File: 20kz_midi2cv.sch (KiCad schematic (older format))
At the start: 27 parts, among them J1 DIN_5, J2 TONE, J3 GATE, J4 GATE, J5 PITCH BEND, J6 power, Q1 2N3904, Q2 2N3904, U1 4N35, U2 ATMEGA328P-PU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

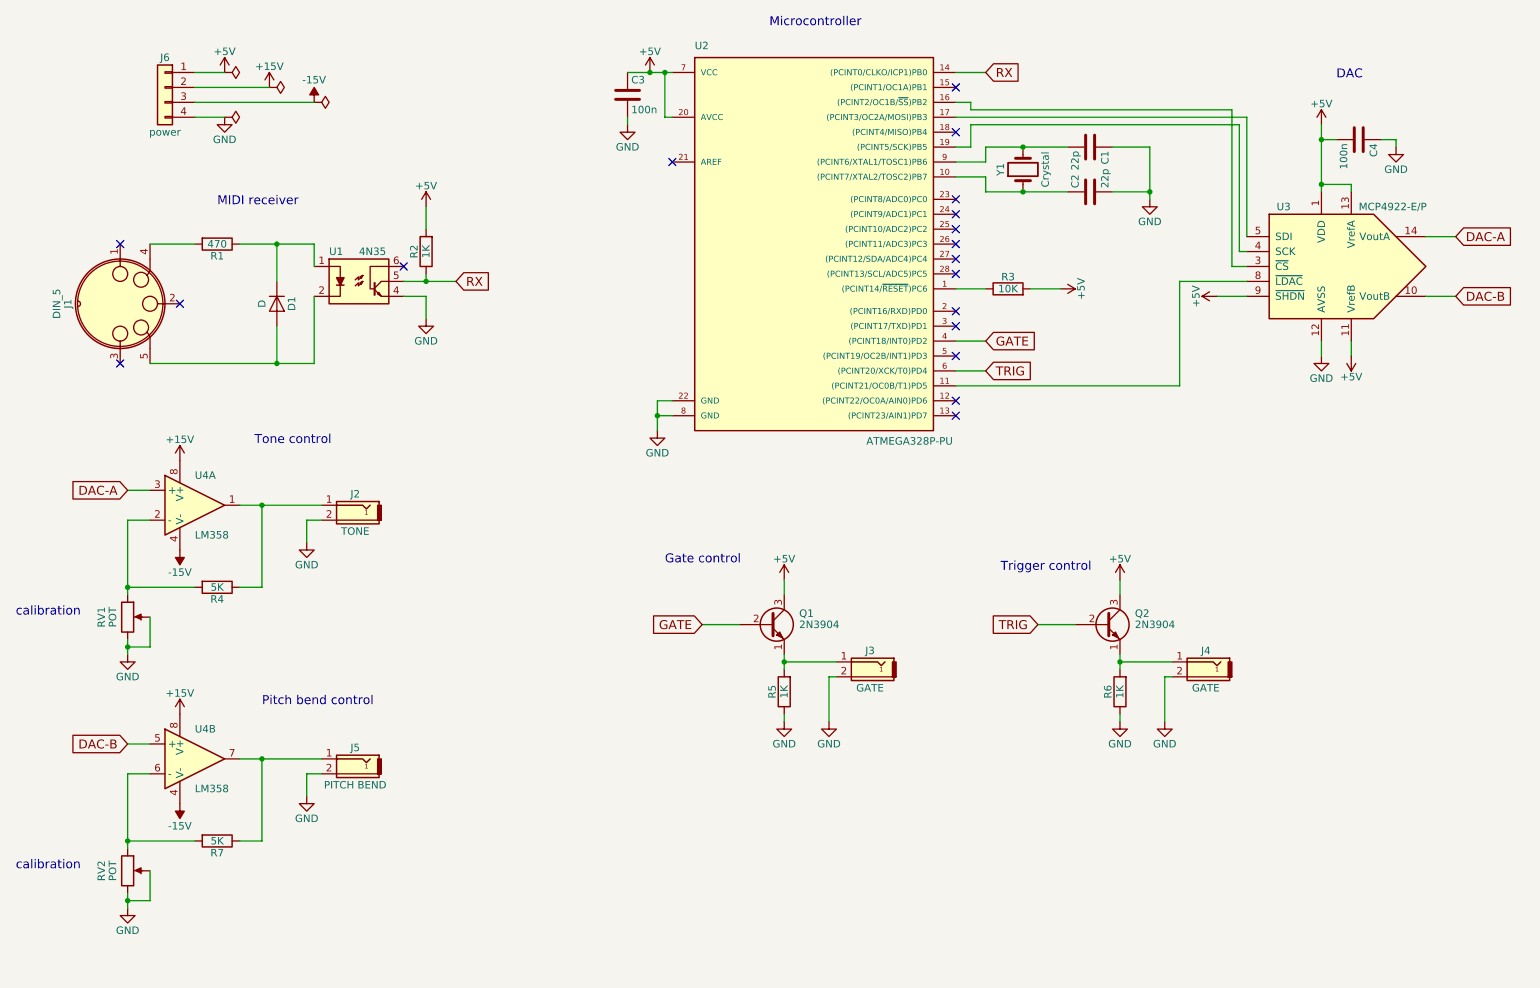
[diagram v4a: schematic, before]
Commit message: el pitch bend control no necesita opamp
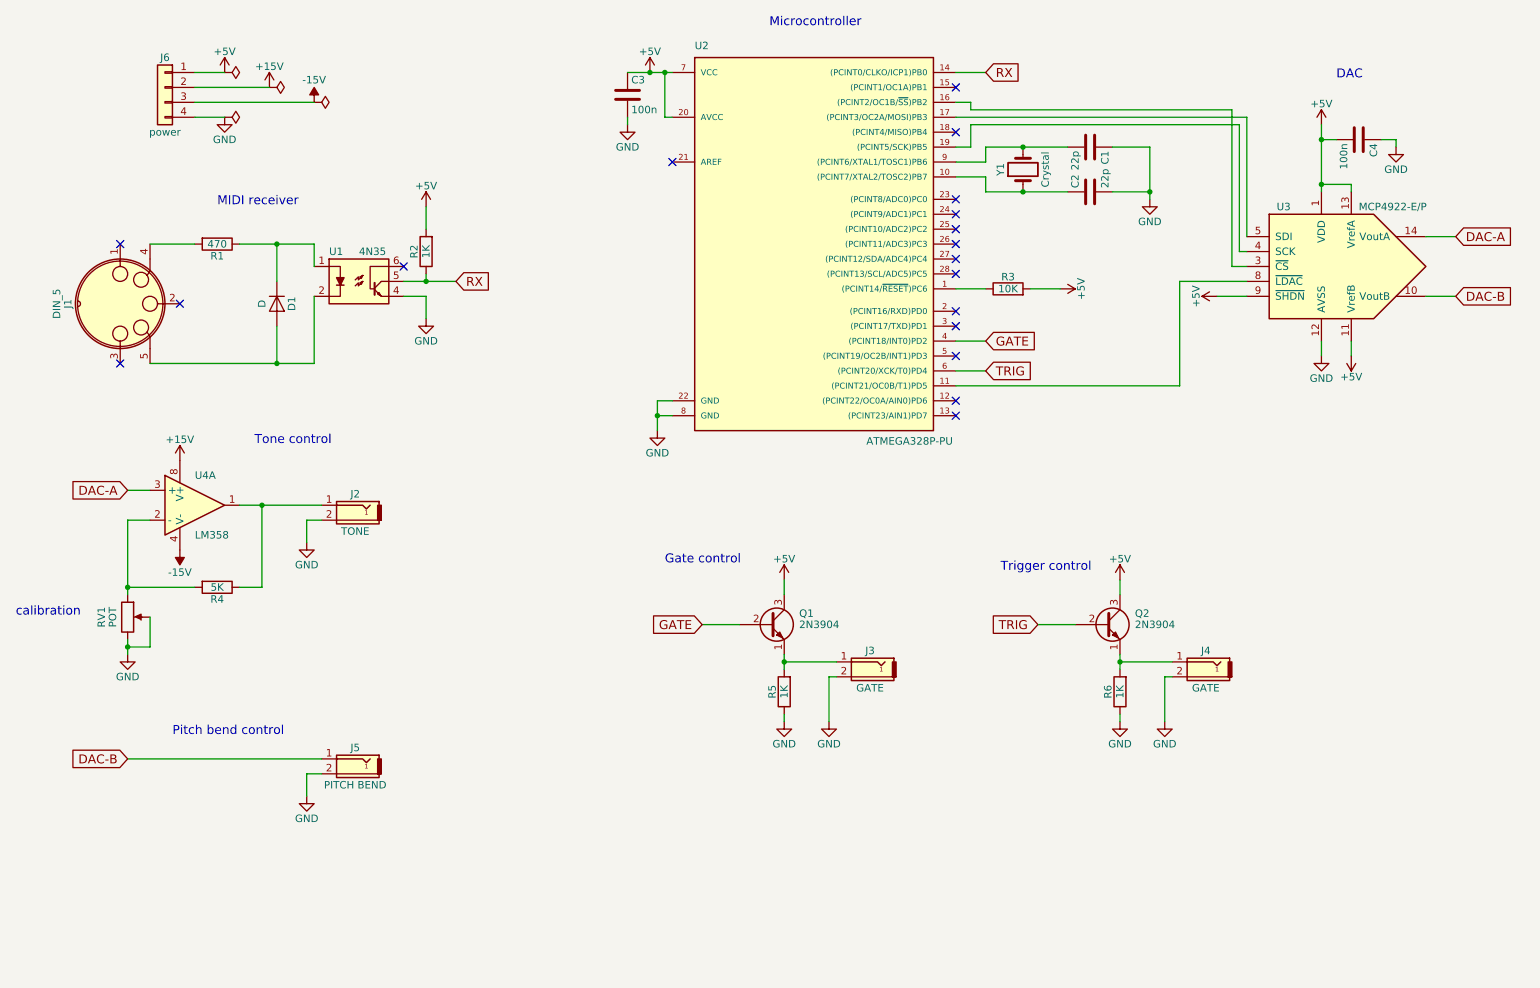
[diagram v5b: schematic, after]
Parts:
- removed R7: 5K, symbol R
- removed RV2: POT, symbol POT
- removed unit 2 of U4
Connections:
- net DAC-B: now also J5.1
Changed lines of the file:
@@
 $EndComp
 $Comp
-L GND #PWR13
+L GND #PWR01
 U 1 1 59BFD3CC
 P 3450 2800
-F 0 "#PWR13" H 3450 2550 50  0001 C CNN
+F 0 "#PWR01" H 3450 2550 50  0001 C CNN
 F 1 "GND" H 3450 2650 50  0000 C CNN
 F 2 "" H 3450 2800 50  0001 C CNN
@@
 $EndComp
 $Comp
-L GND #PWR16
+L GND #PWR02
 U 1 1 59BFDB2E
 P 5000 3550
-F 0 "#PWR16" H 5000 3300 50  0001 C CNN
+F 0 "#PWR02" H 5000 3300 50  0001 C CNN
 F 1 "GND" H 5000 3400 50  0000 C CNN
 F 2 "" H 5000 3550 50  0001 C CNN
@@
 $EndComp
 $Comp
-L GND #PWR9
+L GND #PWR03
 U 1 1 59BFF0AF
 P 8300 2000
-F 0 "#PWR9" H 8300 1750 50  0001 C CNN
+F 0 "#PWR03" H 8300 1750 50  0001 C CNN
 F 1 "GND" H 8300 1850 50  0000 C CNN
 F 2 "" H 8300 2000 50  0001 C CNN
@@
 RX
 $Comp
-L GND #PWR14
+L GND #PWR04
 U 1 1 59C28A87
 P 9450 3050
-F 0 "#PWR14" H 9450 2800 50  0001 C CNN
+F 0 "#PWR04" H 9450 2800 50  0001 C CNN
 F 1 "GND" H 9450 2900 50  0000 C CNN
 F 2 "" H 9450 3050 50  0001 C CNN
@@
 Microcontroller
 $Comp
-L +5V #PWR10
+L +5V #PWR05
 U 1 1 59C2B213
 P 3450 2050
-F 0 "#PWR10" H 3450 1900 50  0001 C CNN
+F 0 "#PWR05" H 3450 1900 50  0001 C CNN
 F 1 "+5V" H 3450 2190 50  0000 C CNN
 F 2 "" H 3450 2050 50  0001 C CNN
@@
 $EndComp
 $Comp
-L +5V #PWR2
+L +5V #PWR06
 U 1 1 59C2B4B2
 P 4950 1150
-F 0 "#PWR2" H 4950 1000 50  0001 C CNN
+F 0 "#PWR06" H 4950 1000 50  0001 C CNN
 F 1 "+5V" H 4950 1290 50  0000 C CNN
 F 2 "" H 4950 1150 50  0001 C CNN
@@
 $EndComp
 $Comp
-L +5V #PWR7
+L +5V #PWR07
 U 1 1 59C2B740
 P 9450 1500
-F 0 "#PWR7" H 9450 1350 50  0001 C CNN
+F 0 "#PWR07" H 9450 1350 50  0001 C CNN
 F 1 "+5V" H 9450 1640 50  0000 C CNN
 F 2 "" H 9450 1500 50  0001 C CNN
@@
 $EndComp
 $Comp
-L +5V #PWR15
+L +5V #PWR08
 U 1 1 59C2B949
 P 9650 3050
-F 0 "#PWR15" H 9650 2900 50  0001 C CNN
+F 0 "#PWR08" H 9650 2900 50  0001 C CNN
 F 1 "+5V" H 9650 3190 50  0000 C CNN
 F 2 "" H 9650 3050 50  0001 C CNN
@@
 $EndComp
 $Comp
-L +5V #PWR11
+L +5V #PWR09
 U 1 1 59C2BF25
 P 7700 2600
-F 0 "#PWR11" H 7700 2450 50  0001 C CNN
+F 0 "#PWR09" H 7700 2450 50  0001 C CNN
 F 1 "+5V" H 7700 2740 50  0000 C CNN
 F 2 "" H 7700 2600 50  0001 C CNN
@@
 $EndComp
 $Comp
-L +5V #PWR12
+L +5V #PWR010
 U 1 1 59C2C020
 P 8750 2650
-F 0 "#PWR12" H 8750 2500 50  0001 C CNN
+F 0 "#PWR010" H 8750 2500 50  0001 C CNN
 F 1 "+5V" H 8750 2790 50  0000 C CNN
 F 2 "" H 8750 2650 50  0001 C CNN
@@
 Connection ~ 9450 1900
 Wire Wire Line
-	9650 1900 9450 1900
+	9450 1900 9650 1900
 Wire Wire Line
 	9650 1950 9650 1900
@@
 $EndComp
 $Comp
-L +15V #PWR17
+L +15V #PWR011
 U 1 1 59C3649C
 P 1800 3750
-F 0 "#PWR17" H 1800 3600 50  0001 C CNN
+F 0 "#PWR011" H 1800 3600 50  0001 C CNN
 F 1 "+15V" H 1800 3890 50  0000 C CNN
 F 2 "" H 1800 3750 50  0001 C CNN
@@
 	10150 2250 10350 2250
 $Comp
-L GND #PWR22
+L GND #PWR012
 U 1 1 59C37211
 P 1450 5050
-F 0 "#PWR22" H 1450 4800 50  0001 C CNN
+F 0 "#PWR012" H 1450 4800 50  0001 C CNN
 F 1 "GND" H 1450 4900 50  0000 C CNN
 F 2 "" H 1450 5050 50  0001 C CNN
@@
 Connection ~ 2350 4050
 $Comp
-L GND #PWR18
+L GND #PWR013
 U 1 1 59C38A05
 P 2650 4300
-F 0 "#PWR18" H 2650 4050 50  0001 C CNN
+F 0 "#PWR013" H 2650 4050 50  0001 C CNN
 F 1 "GND" H 2650 4150 50  0000 C CNN
 F 2 "" H 2650 4300 50  0001 C CNN
@@
 Wire Wire Line
 	2650 4150 2650 4300
-$Comp
-L LM358 U4
-U 2 1 59C38F55
-P 1900 5750
-F 0 "U4" H 1900 5950 50  0000 L CNN
-F 1 "LM358" H 1900 5550 50  0000 L CNN
-F 2 "" H 1900 5750 50  0001 C CNN
-F 3 "" H 1900 5750 50  0001 C CNN
-	2    1900 5750
-	1    0    0    -1
-$EndComp
-$Comp
-L +15V #PWR23
-U 1 1 59C38F5B
-P 1800 5450
-F 0 "#PWR23" H 1800 5300 50  0001 C CNN
-F 1 "+15V" H 1800 5590 50  0000 C CNN
-F 2 "" H 1800 5450 50  0001 C CNN
-F 3 "" H 1800 5450 50  0001 C CNN
-	1    1800 5450
-	1    0    0    -1
-$EndComp
-$Comp
-L -15V #PWR29
-U 1 1 59C38F61
-P 1800 6050
-F 0 "#PWR29" H 1800 6150 50  0001 C CNN
-F 1 "-15V" H 1800 6200 50  0000 C CNN
-F 2 "" H 1800 6050 50  0001 C CNN
-F 3 "" H 1800 6050 50  0001 C CNN
-	1    1800 6050
-	-1   0    0    1
-$EndComp
-Wire Wire Line
-	1800 5450 1800 5450
-Wire Wire Line
-	1800 6050 1800 6050
-$Comp
-L R R7
-U 1 1 59C38F69
-P 2050 6300
-F 0 "R7" V 2130 6300 50  0000 C CNN
-F 1 "5K" V 2050 6300 50  0000 C CNN
-F 2 "" V 1980 6300 50  0001 C CNN
-F 3 "" H 2050 6300 50  0001 C CNN
-	1    2050 6300
-	0    1    1    0
-$EndComp
-$Comp
-L POT RV2
-U 1 1 59C38F6F
-P 1450 6500
-F 0 "RV2" V 1275 6500 50  0000 C CNN
-F 1 "POT" V 1350 6500 50  0000 C CNN
-F 2 "" H 1450 6500 50  0001 C CNN
-F 3 "" H 1450 6500 50  0001 C CNN
-	1    1450 6500
-	1    0    0    -1
-$EndComp
-$Comp
-L GND #PWR30
-U 1 1 59C38F75
-P 1450 6750
-F 0 "#PWR30" H 1450 6500 50  0001 C CNN
-F 1 "GND" H 1450 6600 50  0000 C CNN
-F 2 "" H 1450 6750 50  0001 C CNN
-F 3 "" H 1450 6750 50  0001 C CNN
-	1    1450 6750
-	1    0    0    -1
-$EndComp
-Wire Wire Line
-	1450 6650 1450 6750
-Wire Wire Line
-	1600 6500 1600 6700
-Wire Wire Line
-	1600 6700 1450 6700
-Connection ~ 1450 6700
-Wire Wire Line
-	1600 5850 1450 5850
-Wire Wire Line
-	1450 5850 1450 6350
-Wire Wire Line
-	1900 6300 1450 6300
-Connection ~ 1450 6300
-Wire Wire Line
-	2200 5750 2750 5750
-Wire Wire Line
-	2350 5750 2350 6300
-Wire Wire Line
-	2350 6300 2200 6300
-Wire Wire Line
-	1600 5650 1450 5650
 $Comp
 L Audio-Jack-2 J5
@@
 	-1   0    0    -1
 $EndComp
-Connection ~ 2350 5750
-$Comp
-L GND #PWR28
+$Comp
+L GND #PWR016
 U 1 1 59C38F8F
 P 2650 6000
-F 0 "#PWR28" H 2650 5750 50  0001 C CNN
+F 0 "#PWR016" H 2650 5750 50  0001 C CNN
 F 1 "GND" H 2650 5850 50  0000 C CNN
 F 2 "" H 2650 6000 50  0001 C CNN
@@
 Wire Wire Line
 	2650 5850 2650 6000
-Text GLabel 1450 5650 0    60   Input ~ 0
+Text GLabel 1450 5750 0    60   Input ~ 0
 DAC-B
 Text GLabel 7200 2950 2    60   Input ~ 0
@@
 $EndComp
 $Comp
-L GND #PWR24
+L GND #PWR017
 U 1 1 59C39D84
 P 5850 5500
-F 0 "#PWR24" H 5850 5250 50  0001 C CNN
+F 0 "#PWR017" H 5850 5250 50  0001 C CNN
 F 1 "GND" H 5850 5350 50  0000 C CNN
 F 2 "" H 5850 5500 50  0001 C CNN
@@
 $EndComp
 $Comp
-L +5V #PWR20
+L +5V #PWR018
 U 1 1 59C3A03A
 P 5850 4550
-F 0 "#PWR20" H 5850 4400 50  0001 C CNN
+F 0 "#PWR018" H 5850 4400 50  0001 C CNN
 F 1 "+5V" H 5850 4690 50  0000 C CNN
 F 2 "" H 5850 4550 50  0001 C CNN
@@
 Connection ~ 5850 5100
 $Comp
-L GND #PWR25
+L GND #PWR019
 U 1 1 59C3A4C6
 P 6150 5500
-F 0 "#PWR25" H 6150 5250 50  0001 C CNN
+F 0 "#PWR019" H 6150 5250 50  0001 C CNN
 F 1 "GND" H 6150 5350 50  0000 C CNN
 F 2 "" H 6150 5500 50  0001 C CNN
@@
 $EndComp
 $Comp
-L GND #PWR26
+L GND #PWR020
 U 1 1 59C3A967
 P 8100 5500
-F 0 "#PWR26" H 8100 5250 50  0001 C CNN
+F 0 "#PWR020" H 8100 5250 50  0001 C CNN
 F 1 "GND" H 8100 5350 50  0000 C CNN
 F 2 "" H 8100 5500 50  0001 C CNN
@@
 $EndComp
 $Comp
-L +5V #PWR21
+L +5V #PWR021
 U 1 1 59C3A973
 P 8100 4550
-F 0 "#PWR21" H 8100 4400 50  0001 C CNN
+F 0 "#PWR021" H 8100 4400 50  0001 C CNN
 F 1 "+5V" H 8100 4690 50  0000 C CNN
 F 2 "" H 8100 4550 50  0001 C CNN
@@
 Connection ~ 8100 5100
 $Comp
-L GND #PWR27
+L GND #PWR022
 U 1 1 59C3A985
 P 8400 5500
-F 0 "#PWR27" H 8400 5250 50  0001 C CNN
+F 0 "#PWR022" H 8400 5250 50  0001 C CNN
 F 1 "GND" H 8400 5350 50  0000 C CNN
 F 2 "" H 8400 5500 50  0001 C CNN
@@
 Text Notes 2300 3650 0    60   ~ 0
 Tone control
-Text Notes 2350 5400 0    60   ~ 0
+Text Notes 1750 5600 0    60   ~ 0
 Pitch bend control
 Text Notes 5050 4450 0    60   ~ 0
@@
 Text Notes 7300 4500 0    60   ~ 0
 Trigger control
-Text Notes 700  6500 0    60   ~ 0
-calibration
 Text Notes 700  4800 0    60   ~ 0
 calibration
@@
 $EndComp
 $Comp
-L +5V #PWR1
+L +5V #PWR023
 U 1 1 59C3CE9F
 P 2100 1150
-F 0 "#PWR1" H 2100 1000 50  0001 C CNN
+F 0 "#PWR023" H 2100 1000 50  0001 C CNN
 F 1 "+5V" H 2100 1290 50  0000 C CNN
 F 2 "" H 2100 1150 50  0001 C CNN
@@
 $EndComp
 $Comp
-L +15V #PWR3
+L +15V #PWR024
 U 1 1 59C3CF60
 P 2400 1250
-F 0 "#PWR3" H 2400 1100 50  0001 C CNN
+F 0 "#PWR024" H 2400 1100 50  0001 C CNN
 F 1 "+15V" H 2400 1390 50  0000 C CNN
 F 2 "" H 2400 1250 50  0001 C CNN
@@
 $EndComp
 $Comp
-L GND #PWR5
+L GND #PWR025
 U 1 1 59C3D43E
 P 2100 1450
-F 0 "#PWR5" H 2100 1200 50  0001 C CNN
+F 0 "#PWR025" H 2100 1200 50  0001 C CNN
 F 1 "GND" H 2100 1300 50  0000 C CNN
 F 2 "" H 2100 1450 50  0001 C CNN
@@
 	1900 1450 2100 1450
 $Comp
-L PWR_FLAG #FLG1
+L PWR_FLAG #FLG026
 U 1 1 59C3DC74
 P 2100 1150
-F 0 "#FLG1" H 2100 1225 50  0001 C CNN
+F 0 "#FLG026" H 2100 1225 50  0001 C CNN
 F 1 "PWR_FLAG" H 2100 1300 50  0001 C CNN
 F 2 "" H 2100 1150 50  0001 C CNN
@@
 $EndComp
 $Comp
-L PWR_FLAG #FLG2
+L PWR_FLAG #FLG027
 U 1 1 59C3DD8A
 P 2400 1250
-F 0 "#FLG2" H 2400 1325 50  0001 C CNN
+F 0 "#FLG027" H 2400 1325 50  0001 C CNN
 F 1 "PWR_FLAG" H 2400 1400 50  0001 C CNN
 F 2 "" H 2400 1250 50  0001 C CNN
@@
 $EndComp
 $Comp
-L PWR_FLAG #FLG3
+L PWR_FLAG #FLG028
 U 1 1 59C3DDE3
 P 2700 1350
-F 0 "#FLG3" H 2700 1425 50  0001 C CNN
+F 0 "#FLG028" H 2700 1425 50  0001 C CNN
 F 1 "PWR_FLAG" H 2700 1500 50  0001 C CNN
 F 2 "" H 2700 1350 50  0001 C CNN
@@
 $EndComp
 $Comp
-L PWR_FLAG #FLG4
+L PWR_FLAG #FLG029
 U 1 1 59C3DFB5
 P 2100 1450
-F 0 "#FLG4" H 2100 1525 50  0001 C CNN
+F 0 "#FLG029" H 2100 1525 50  0001 C CNN
 F 1 "PWR_FLAG" H 2100 1600 50  0001 C CNN
 F 2 "" H 2100 1450 50  0001 C CNN
@@
 $EndComp
 $Comp
-L GND #PWR6
+L GND #PWR030
 U 1 1 59C4ECB6
 P 4800 1500
-F 0 "#PWR6" H 4800 1250 50  0001 C CNN
+F 0 "#PWR030" H 4800 1250 50  0001 C CNN
 F 1 "GND" H 4800 1350 50  0000 C CNN
 F 2 "" H 4800 1500 50  0001 C CNN
@@
 $EndComp
 $Comp
-L GND #PWR8
+L GND #PWR031
 U 1 1 59C4F19E
 P 9950 1650
-F 0 "#PWR8" H 9950 1400 50  0001 C CNN
+F 0 "#PWR031" H 9950 1400 50  0001 C CNN
 F 1 "GND" H 9950 1500 50  0000 C CNN
 F 2 "" H 9950 1650 50  0001 C CNN
@@
 	9550 1600 9450 1600
 Connection ~ 9450 1600
+Wire Wire Line
+	1450 5750 2750 5750
 $EndSCHEMATC
